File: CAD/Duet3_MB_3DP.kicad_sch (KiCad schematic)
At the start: 0 parts

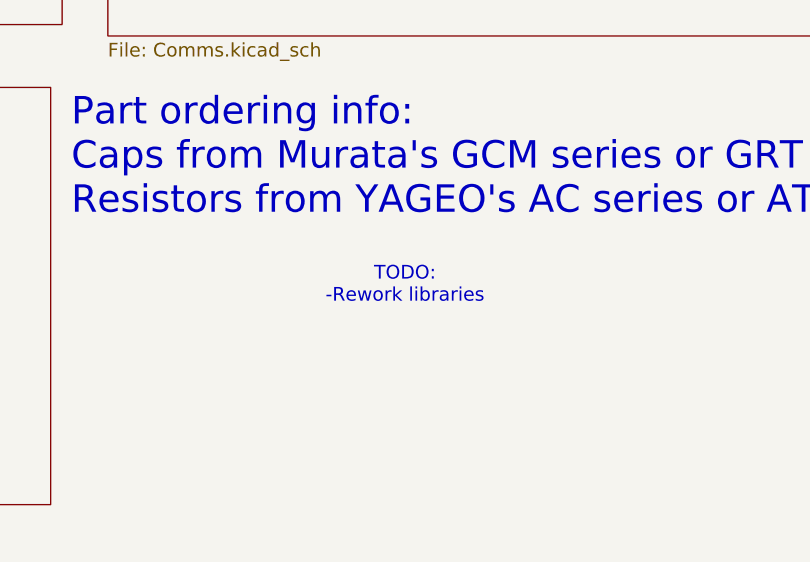
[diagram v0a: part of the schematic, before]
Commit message: No physical board changes
Update a datasheet
removed a comment (Carter reworked the libraries a while - thanks Carter)
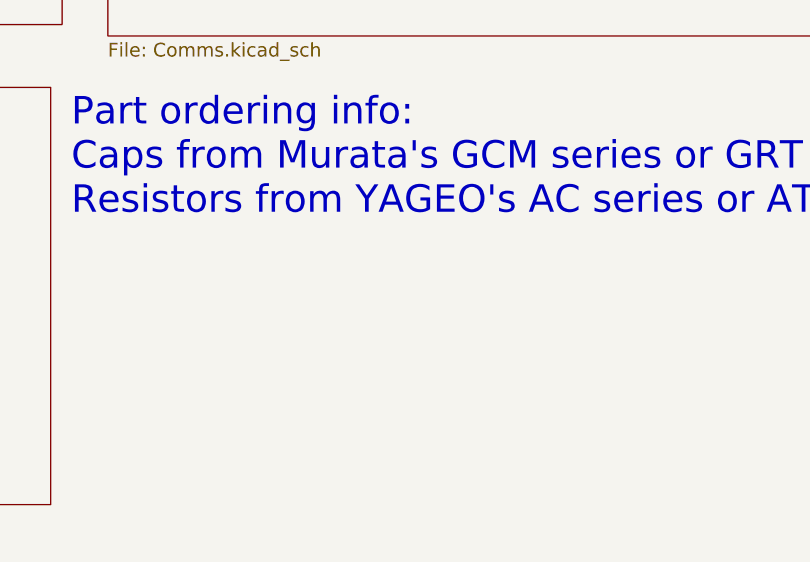
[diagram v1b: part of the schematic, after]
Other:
- note removed: "TODO: -Rework libraries"
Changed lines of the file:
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@@
 		(comment 1 "(c) 3DPotter")
-	)
-	(text "TODO:\n-Rework libraries\n "
-		(exclude_from_sim no)
-		(at 138.43 168.656 0)
-		(effects
-			(font
-				(size 1.524 1.524)
-			)
-		)
 	)
 	(text "Duet3 Mainboard 3DP"

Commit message: Finalize changes for 1.56
LCSC and P/N updated for excessively out of stock parts.
Silkscreen changes so no more DRC errors
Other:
- title: Duet 3 Main Board 3DP -> Duet 3 MB 3DP
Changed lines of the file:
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@@
 	(paper "A3" portrait)
 	(title_block
-		(title "Duet 3 Main Board 3DP")
-		(date "2026-02-17")
-		(rev "1.55")
+		(title "Duet 3 MB 3DP")
+		(date "2026-06-02")
+		(rev "1.56")
 		(company "3DPotter")
 		(comment 1 "(c) 3DPotter")
